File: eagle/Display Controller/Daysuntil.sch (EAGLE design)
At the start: 45 parts, among them IC1 DS1307, IC2 ATMEGA168-20P, IC3 74HC595N, IC4 74HC595N, IC5 7805TV, Q1 32.768 kHz, T1 BC337, T10 BC337, T11 BC337, T12 BC337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

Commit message: updated board config
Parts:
- C1, C4, C5, C6: value 10uF -> 0.1uF
- C2, C3: value 10uF -> 100uF
- U$2: value (none) -> 16MHz
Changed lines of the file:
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@@
 <part name="P+6" library="supply1" deviceset="VCC" device=""/>
 <part name="P+7" library="supply1" deviceset="VCC" device=""/>
-<part name="U$2" library="adafruit" deviceset="CERMOSCILL" device="-THM"/>
+<part name="U$2" library="adafruit" deviceset="CERMOSCILL" device="-THM" value="16MHz"/>
 <part name="GND8" library="supply1" deviceset="GND" device=""/>
 <part name="P+8" library="supply1" deviceset="VCC" device=""/>
@@
 <part name="P+24" library="supply1" deviceset="+12V" device=""/>
 <part name="IC5" library="linear" deviceset="78*" device="TV" technology="05"/>
-<part name="C2" library="adafruit" deviceset="C-US" device="050-050X075" value="10uF"/>
-<part name="C3" library="adafruit" deviceset="C-US" device="050-050X075" value="10uF"/>
+<part name="C2" library="adafruit" deviceset="C-US" device="050-050X075" value="100uF"/>
+<part name="C3" library="adafruit" deviceset="C-US" device="050-050X075" value="100uF"/>
 <part name="P+25" library="supply1" deviceset="VCC" device=""/>
 <part name="JP1" library="pinhead" deviceset="PINHD-1X16" device="" value="Output"/>
 <part name="P+26" library="supply1" deviceset="+12V" device=""/>
 <part name="GND23" library="supply1" deviceset="GND" device=""/>
-<part name="C1" library="adafruit" deviceset="C-US" device="025-030X050" value="10uF"/>
-<part name="C4" library="adafruit" deviceset="C-US" device="025-030X050" value="10uF"/>
-<part name="C6" library="adafruit" deviceset="C-US" device="025-030X050" value="10uF"/>
-<part name="C5" library="adafruit" deviceset="C-US" device="025-030X050" value="10uF"/>
+<part name="C1" library="adafruit" deviceset="C-US" device="025-030X050" value="0.1uF"/>
+<part name="C4" library="adafruit" deviceset="C-US" device="025-030X050" value="0.1uF"/>
+<part name="C6" library="adafruit" deviceset="C-US" device="025-030X050" value="0.1uF"/>
+<part name="C5" library="adafruit" deviceset="C-US" device="025-030X050" value="0.1uF"/>
 <part name="P+1" library="supply1" deviceset="VCC" device=""/>
 <part name="GND3" library="supply1" deviceset="GND" device=""/>

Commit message: finalized board design
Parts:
- added SL1: (no value), con-amp-quick:M02
- IC2: value ATMEGA168-20P -> ATMEGA328P
- JP1: value Output -> (none); device pinhead:PINHD-1X16 -> pinhead:PINHD-1X14
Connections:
- net +12V: now also SL1.2; no longer JP1.16
- net GND: now also SL1.1; no longer JP1.15
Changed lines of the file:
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@@
 <part name="Q1" library="crystal" deviceset="CRYSTAL" device="TC38H" value="32.768 kHz"/>
 <part name="IC1" library="adafruit" deviceset="DS1307" device=""/>
-<part name="IC2" library="adafruit" deviceset="ATMEGA168*P" device="" technology="-20"/>
+<part name="IC2" library="adafruit" deviceset="ATMEGA168*P" device="" technology="-20" value="ATMEGA328P"/>
 <part name="P+3" library="supply1" deviceset="VCC" device=""/>
 <part name="P+5" library="supply1" deviceset="VCC" device=""/>
@@
 <part name="C3" library="adafruit" deviceset="C-US" device="050-050X075" value="100uF"/>
 <part name="P+25" library="supply1" deviceset="VCC" device=""/>
-<part name="JP1" library="pinhead" deviceset="PINHD-1X16" device="" value="Output"/>
 <part name="P+26" library="supply1" deviceset="+12V" device=""/>
 <part name="GND23" library="supply1" deviceset="GND" device=""/>
@@
 <part name="GND3" library="supply1" deviceset="GND" device=""/>
 <part name="GND1" library="supply1" deviceset="GND" device=""/>
+<part name="JP1" library="pinhead" deviceset="PINHD-1X14" device=""/>
+<part name="SL1" library="con-amp-quick" deviceset="M02" device=""/>
 </parts>
 <sheets>
@@
 <instance part="C3" gate="G$1" x="93.98" y="22.86"/>
 <instance part="P+25" gate="VCC" x="93.98" y="38.1"/>
-<instance part="JP1" gate="A" x="137.16" y="25.4" rot="R90"/>
-<instance part="P+26" gate="1" x="160.02" y="7.62" rot="R270"/>
-<instance part="GND23" gate="1" x="154.94" y="5.08"/>
+<instance part="P+26" gate="1" x="167.64" y="10.16" rot="R270"/>
+<instance part="GND23" gate="1" x="162.56" y="10.16"/>
 <instance part="C1" gate="G$1" x="48.26" y="96.52" rot="R180"/>
 <instance part="C4" gate="G$1" x="40.64" y="81.28" rot="R90"/>
@@
 <instance part="GND3" gate="1" x="45.72" y="101.6" rot="R270"/>
 <instance part="GND1" gate="1" x="30.48" y="40.64"/>
+<instance part="JP1" gate="A" x="134.62" y="25.4" rot="R90"/>
+<instance part="SL1" gate="G$1" x="162.56" y="22.86" rot="R270"/>
 </instances>
 <busses>
@@
 </segment>
 <segment>
-<pinref part="JP1" gate="A" pin="15"/>
 <pinref part="GND23" gate="1" pin="GND"/>
-<wire x1="154.94" y1="7.62" x2="154.94" y2="22.86" width="0.1524" layer="91"/>
+<wire x1="162.56" y1="12.7" x2="162.56" y2="15.24" width="0.1524" layer="91"/>
+<pinref part="SL1" gate="G$1" pin="1"/>
 </segment>
 <segment>
@@
 </segment>
 <segment>
-<pinref part="JP1" gate="A" pin="16"/>
 <pinref part="P+26" gate="1" pin="+12V"/>
-<wire x1="157.48" y1="7.62" x2="157.48" y2="22.86" width="0.1524" layer="91"/>
+<wire x1="165.1" y1="10.16" x2="165.1" y2="15.24" width="0.1524" layer="91"/>
+<pinref part="SL1" gate="G$1" pin="2"/>
 </segment>
 </net>
@@
 </segment>
 <segment>
-<pinref part="JP1" gate="A" pin="1"/>
 <wire x1="119.38" y1="22.86" x2="119.38" y2="12.7" width="0.1524" layer="91"/>
 <label x="119.38" y="12.7" size="1.778" layer="95" rot="R90"/>
+<pinref part="JP1" gate="A" pin="1"/>
 </segment>
 </net>
@@
 </segment>
 <segment>
-<pinref part="JP1" gate="A" pin="2"/>
 <wire x1="121.92" y1="22.86" x2="121.92" y2="12.7" width="0.1524" layer="91"/>
 <label x="121.92" y="12.7" size="1.778" layer="95" rot="R90"/>
+<pinref part="JP1" gate="A" pin="2"/>
 </segment>
 </net>
@@
 </segment>
 <segment>
-<pinref part="JP1" gate="A" pin="3"/>
 <wire x1="124.46" y1="22.86" x2="124.46" y2="12.7" width="0.1524" layer="91"/>
 <label x="124.46" y="12.7" size="1.778" layer="95" rot="R90"/>
+<pinref part="JP1" gate="A" pin="3"/>
 </segment>
 </net>
@@
 </segment>
 <segment>
-<pinref part="JP1" gate="A" pin="4"/>
 <wire x1="127" y1="22.86" x2="127" y2="12.7" width="0.1524" layer="91"/>
 <label x="127" y="12.7" size="1.778" layer="95" rot="R90"/>
+<pinref part="JP1" gate="A" pin="4"/>
 </segment>
 </net>
@@
 </segment>
 <segment>
-<pinref part="JP1" gate="A" pin="5"/>
 <wire x1="129.54" y1="22.86" x2="129.54" y2="12.7" width="0.1524" layer="91"/>
 <label x="129.54" y="12.7" size="1.778" layer="95" rot="R90"/>
+<pinref part="JP1" gate="A" pin="5"/>
 </segment>
 </net>
@@
 </segment>
 <segment>
-<pinref part="JP1" gate="A" pin="6"/>
 <wire x1="132.08" y1="22.86" x2="132.08" y2="12.7" width="0.1524" layer="91"/>
 <label x="132.08" y="12.7" size="1.778" layer="95" rot="R90"/>
+<pinref part="JP1" gate="A" pin="6"/>
 </segment>
 </net>
@@
 </segment>
 <segment>
-<pinref part="JP1" gate="A" pin="7"/>
 <wire x1="134.62" y1="22.86" x2="134.62" y2="12.7" width="0.1524" layer="91"/>
 <label x="134.62" y="12.7" size="1.778" layer="95" rot="R90"/>
+<pinref part="JP1" gate="A" pin="7"/>
 </segment>
 </net>
@@
 </segment>
 <segment>
-<pinref part="JP1" gate="A" pin="14"/>
 <wire x1="152.4" y1="22.86" x2="152.4" y2="12.7" width="0.1524" layer="91"/>
 <label x="152.4" y="12.7" size="1.778" layer="95" rot="R90"/>
+<pinref part="JP1" gate="A" pin="14"/>
 </segment>
 </net>
@@
 </segment>
 <segment>
-<pinref part="JP1" gate="A" pin="13"/>
 <wire x1="149.86" y1="22.86" x2="149.86" y2="12.7" width="0.1524" layer="91"/>
 <label x="149.86" y="12.7" size="1.778" layer="95" rot="R90"/>
+<pinref part="JP1" gate="A" pin="13"/>
 </segment>
 </net>
@@
 </segment>
 <segment>
-<pinref part="JP1" gate="A" pin="12"/>
 <wire x1="147.32" y1="22.86" x2="147.32" y2="12.7" width="0.1524" layer="91"/>
 <label x="147.32" y="12.7" size="1.778" layer="95" rot="R90"/>
+<pinref part="JP1" gate="A" pin="12"/>
 </segment>
 </net>
@@
 </segment>
 <segment>
-<pinref part="JP1" gate="A" pin="11"/>
 <wire x1="144.78" y1="22.86" x2="144.78" y2="12.7" width="0.1524" layer="91"/>
 <label x="144.78" y="12.7" size="1.778" layer="95" rot="R90"/>
+<pinref part="JP1" gate="A" pin="11"/>
 </segment>
 </net>
@@
 </segment>
 <segment>
-<pinref part="JP1" gate="A" pin="10"/>
 <wire x1="142.24" y1="22.86" x2="142.24" y2="12.7" width="0.1524" layer="91"/>
 <label x="142.24" y="12.7" size="1.778" layer="95" rot="R90"/>
+<pinref part="JP1" gate="A" pin="10"/>
 </segment>
 </net>
@@
 </segment>
 <segment>
-<pinref part="JP1" gate="A" pin="9"/>
 <wire x1="139.7" y1="22.86" x2="139.7" y2="12.7" width="0.1524" layer="91"/>
 <label x="139.7" y="12.7" size="1.778" layer="95" rot="R90"/>
+<pinref part="JP1" gate="A" pin="9"/>
 </segment>
 </net>
@@
 </segment>
 <segment>
-<pinref part="JP1" gate="A" pin="8"/>
 <wire x1="137.16" y1="22.86" x2="137.16" y2="12.7" width="0.1524" layer="91"/>
 <label x="137.16" y="12.7" size="1.778" layer="95" rot="R90"/>
-</segment>
-</net>
+<pinref part="JP1" gate="A" pin="8"/>
+</segment>
+</net>

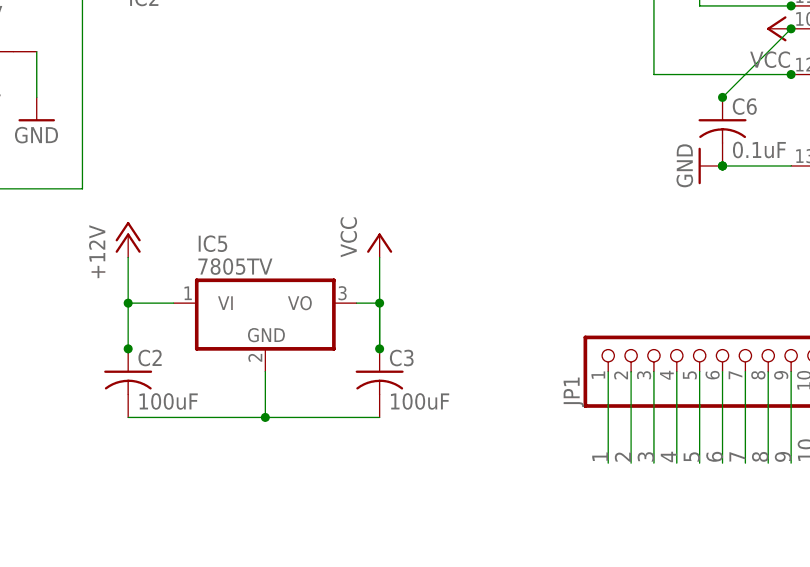
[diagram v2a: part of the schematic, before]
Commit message: final board design with CAM files
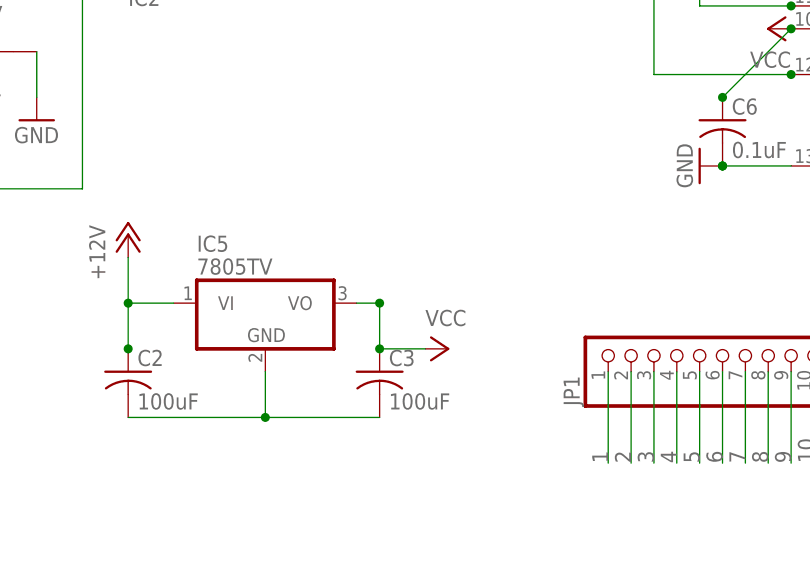
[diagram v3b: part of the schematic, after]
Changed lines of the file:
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@@
 <instance part="C2" gate="G$1" x="66.04" y="22.86"/>
 <instance part="C3" gate="G$1" x="93.98" y="22.86"/>
-<instance part="P+25" gate="VCC" x="93.98" y="38.1"/>
+<instance part="P+25" gate="VCC" x="101.6" y="25.4" rot="R270"/>
 <instance part="P+26" gate="1" x="167.64" y="10.16" rot="R270"/>
 <instance part="GND23" gate="1" x="162.56" y="10.16"/>
@@
 </segment>
 <segment>
-<pinref part="IC5" gate="A1" pin="VO"/>
-<wire x1="91.44" y1="30.48" x2="93.98" y2="30.48" width="0.1524" layer="91"/>
-<pinref part="C3" gate="G$1" pin="1"/>
-<wire x1="93.98" y1="30.48" x2="93.98" y2="25.4" width="0.1524" layer="91"/>
-<wire x1="93.98" y1="25.4" x2="93.98" y2="30.48" width="0.1524" layer="91"/>
-<junction x="93.98" y="30.48"/>
-<wire x1="93.98" y1="30.48" x2="93.98" y2="35.56" width="0.1524" layer="91"/>
-<pinref part="P+25" gate="VCC" pin="VCC"/>
-<junction x="93.98" y="25.4"/>
-</segment>
-<segment>
 <pinref part="C1" gate="G$1" pin="1"/>
 <pinref part="IC2" gate="G$1" pin="VCC"/>
@@
 <pinref part="P+1" gate="VCC" pin="VCC"/>
 </segment>
-</net>
+<segment>
+<pinref part="IC5" gate="A1" pin="VO"/>
+<wire x1="91.44" y1="30.48" x2="93.98" y2="30.48" width="0.1524" layer="91"/>
+<pinref part="C3" gate="G$1" pin="1"/>
+<wire x1="93.98" y1="25.4" x2="93.98" y2="30.48" width="0.1524" layer="91"/>
+<junction x="93.98" y="25.4"/>
+<pinref part="P+25" gate="VCC" pin="VCC"/>
+<wire x1="93.98" y1="25.4" x2="99.06" y2="25.4" width="0.1524" layer="91"/>
+<junction x="93.98" y="30.48"/>
+</segment>
+</net>

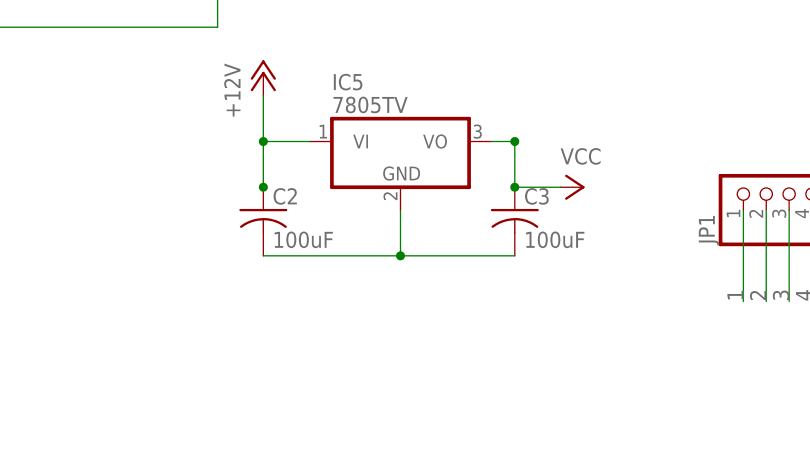
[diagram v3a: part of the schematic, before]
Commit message: upload code v1 and fix ground on 7805 in board schematic.
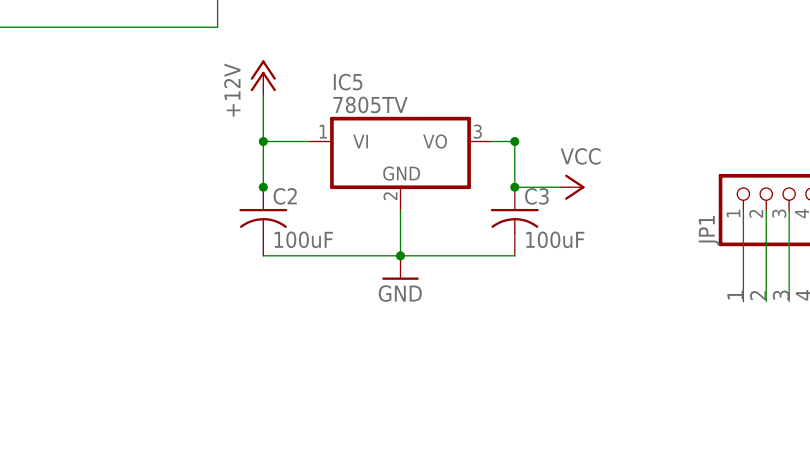
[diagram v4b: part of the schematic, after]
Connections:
- removed net N$23: C2.2, C3.2, IC5.GND
- net GND: now also C2.2, C3.2, IC5.GND
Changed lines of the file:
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@@
 <part name="JP1" library="pinhead" deviceset="PINHD-1X14" device=""/>
 <part name="SL1" library="con-amp-quick" deviceset="M02" device=""/>
+<part name="GND4" library="supply1" deviceset="GND" device=""/>
 </parts>
 <sheets>
@@
 <instance part="JP1" gate="A" x="134.62" y="25.4" rot="R90"/>
 <instance part="SL1" gate="G$1" x="162.56" y="22.86" rot="R270"/>
+<instance part="GND4" gate="1" x="81.28" y="15.24"/>
 </instances>
 <busses>
@@
 <pinref part="GND1" gate="1" pin="GND"/>
 <junction x="30.48" y="43.18"/>
+</segment>
+<segment>
+<pinref part="C2" gate="G$1" pin="2"/>
+<wire x1="66.04" y1="17.78" x2="81.28" y2="17.78" width="0.1524" layer="91"/>
+<pinref part="IC5" gate="A1" pin="GND"/>
+<wire x1="81.28" y1="17.78" x2="81.28" y2="22.86" width="0.1524" layer="91"/>
+<pinref part="C3" gate="G$1" pin="2"/>
+<wire x1="93.98" y1="17.78" x2="81.28" y2="17.78" width="0.1524" layer="91"/>
+<junction x="81.28" y="17.78"/>
+<pinref part="GND4" gate="1" pin="GND"/>
 </segment>
 </net>
@@
 </segment>
 </net>
-<net name="N$23" class="0">
-<segment>
-<pinref part="C2" gate="G$1" pin="2"/>
-<wire x1="66.04" y1="17.78" x2="81.28" y2="17.78" width="0.1524" layer="91"/>
-<pinref part="IC5" gate="A1" pin="GND"/>
-<wire x1="81.28" y1="17.78" x2="81.28" y2="22.86" width="0.1524" layer="91"/>
-<pinref part="C3" gate="G$1" pin="2"/>
-<wire x1="93.98" y1="17.78" x2="81.28" y2="17.78" width="0.1524" layer="91"/>
-<junction x="81.28" y="17.78"/>
-</segment>
-</net>
